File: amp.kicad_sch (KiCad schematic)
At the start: 13 parts, among them J12 JST_SH_1x2_SM02B-SRSS-TB-LF-SN, J9 JST_SUR_1x5_BM05B-SURS-TB-LF-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, U17 MAX98357A

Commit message: [#71249] Update project name
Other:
- title: Audio Latency Processing Board -> Audio controller board
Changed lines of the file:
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@@
 	(paper "A3")
 	(title_block
-		(title "Audio Latency Processing Board")
+		(title "Audio controller board")
 		(date "2025-01-20")
 		(rev "1.2.0")
@@
 		)
 		(instances
-			(project "audio-latency-processing-board"
+			(project "audio-controller-board"
 				(path "/7fb12ebf-f685-4412-b638-445b1bf344bc/80300fa7-dce3-4149-8e27-6609cbfb608d"
 					(reference "R36")
@@
 		)
 		(instances
-			(project "audio-latency-processing-board"
+			(project "audio-controller-board"
 				(path "/7fb12ebf-f685-4412-b638-445b1bf344bc/80300fa7-dce3-4149-8e27-6609cbfb608d"
 					(reference "D10")
@@
 		)
 		(instances
-			(project "audio-latency-processing-board"
+			(project "audio-controller-board"
 				(path "/7fb12ebf-f685-4412-b638-445b1bf344bc/80300fa7-dce3-4149-8e27-6609cbfb608d"
 					(reference "#PWR0138")
@@
 		)
 		(instances
-			(project "audio-latency-processing-board"
+			(project "audio-controller-board"
 				(path "/7fb12ebf-f685-4412-b638-445b1bf344bc/80300fa7-dce3-4149-8e27-6609cbfb608d"
 					(reference "J9")
@@
 		)
 		(instances
-			(project "audio-latency-processing-board"
+			(project "audio-controller-board"
 				(path "/7fb12ebf-f685-4412-b638-445b1bf344bc/80300fa7-dce3-4149-8e27-6609cbfb608d"
 					(reference "#PWR0139")
@@
 		)
 		(instances
-			(project "audio-latency-processing-board"
+			(project "audio-controller-board"
 				(path "/7fb12ebf-f685-4412-b638-445b1bf344bc/80300fa7-dce3-4149-8e27-6609cbfb608d"
 					(reference "#PWR036")
@@
 		)
 		(instances
-			(project "audio-latency-processing-board"
+			(project "audio-controller-board"
 				(path "/7fb12ebf-f685-4412-b638-445b1bf344bc/80300fa7-dce3-4149-8e27-6609cbfb608d"
 					(reference "#PWR0127")
@@
 		)
 		(instances
-			(project "audio-latency-processing-board"
+			(project "audio-controller-board"
 				(path "/7fb12ebf-f685-4412-b638-445b1bf344bc/80300fa7-dce3-4149-8e27-6609cbfb608d"
 					(reference "#PWR033")
@@
 		)
 		(instances
-			(project "audio-latency-processing-board"
+			(project "audio-controller-board"
 				(path "/7fb12ebf-f685-4412-b638-445b1bf344bc/80300fa7-dce3-4149-8e27-6609cbfb608d"
 					(reference "#PWR067")
@@
 		)
 		(instances
-			(project "audio-latency-processing-board"
+			(project "audio-controller-board"
 				(path "/7fb12ebf-f685-4412-b638-445b1bf344bc/80300fa7-dce3-4149-8e27-6609cbfb608d"
 					(reference "D11")
@@
 		)
 		(instances
-			(project "audio-latency-processing-board"
+			(project "audio-controller-board"
 				(path "/7fb12ebf-f685-4412-b638-445b1bf344bc/80300fa7-dce3-4149-8e27-6609cbfb608d"
 					(reference "#PWR0160")
@@
 		)
 		(instances
-			(project "audio-latency-processing-board"
+			(project "audio-controller-board"
 				(path "/7fb12ebf-f685-4412-b638-445b1bf344bc/80300fa7-dce3-4149-8e27-6609cbfb608d"
 					(reference "#PWR041")
@@
 		)
 		(instances
-			(project "audio-latency-processing-board"
+			(project "audio-controller-board"
 				(path "/7fb12ebf-f685-4412-b638-445b1bf344bc/80300fa7-dce3-4149-8e27-6609cbfb608d"
 					(reference "R99")
@@
 		)
 		(instances
-			(project "audio-latency-processing-board"
+			(project "audio-controller-board"
 				(path "/7fb12ebf-f685-4412-b638-445b1bf344bc/80300fa7-dce3-4149-8e27-6609cbfb608d"
 					(reference "#PWR032")
@@
 		)
 		(instances
-			(project "audio-latency-processing-board"
+			(project "audio-controller-board"
 				(path "/7fb12ebf-f685-4412-b638-445b1bf344bc/80300fa7-dce3-4149-8e27-6609cbfb608d"
 					(reference "#PWR0128")
@@
 		)
 		(instances
-			(project "audio-latency-processing-board"
+			(project "audio-controller-board"
 				(path "/7fb12ebf-f685-4412-b638-445b1bf344bc/80300fa7-dce3-4149-8e27-6609cbfb608d"
 					(reference "#PWR0129")
@@
 		)
 		(instances
-			(project "audio-latency-processing-board"
+			(project "audio-controller-board"
 				(path "/7fb12ebf-f685-4412-b638-445b1bf344bc/80300fa7-dce3-4149-8e27-6609cbfb608d"
 					(reference "C53")
@@
 		)
 		(instances
-			(project "audio-latency-processing-board"
+			(project "audio-controller-board"
 				(path "/7fb12ebf-f685-4412-b638-445b1bf344bc/80300fa7-dce3-4149-8e27-6609cbfb608d"
 					(reference "#PWR037")
@@
 		)
 		(instances
-			(project "audio-latency-processing-board"
+			(project "audio-controller-board"
 				(path "/7fb12ebf-f685-4412-b638-445b1bf344bc/80300fa7-dce3-4149-8e27-6609cbfb608d"
 					(reference "#PWR0140")
@@
 		)
 		(instances
-			(project "audio-latency-processing-board"
+			(project "audio-controller-board"
 				(path "/7fb12ebf-f685-4412-b638-445b1bf344bc/80300fa7-dce3-4149-8e27-6609cbfb608d"
 					(reference "R17")
@@
 		)
 		(instances
-			(project "audio-latency-processing-board"
+			(project "audio-controller-board"
 				(path "/7fb12ebf-f685-4412-b638-445b1bf344bc/80300fa7-dce3-4149-8e27-6609cbfb608d"
 					(reference "D12")
@@
 		)
 		(instances
-			(project "audio-latency-processing-board"
+			(project "audio-controller-board"
 				(path "/7fb12ebf-f685-4412-b638-445b1bf344bc/80300fa7-dce3-4149-8e27-6609cbfb608d"
 					(reference "#PWR034")
@@
 		)
 		(instances
-			(project "audio-latency-processing-board"
+			(project "audio-controller-board"
 				(path "/7fb12ebf-f685-4412-b638-445b1bf344bc/80300fa7-dce3-4149-8e27-6609cbfb608d"
 					(reference "#PWR065")

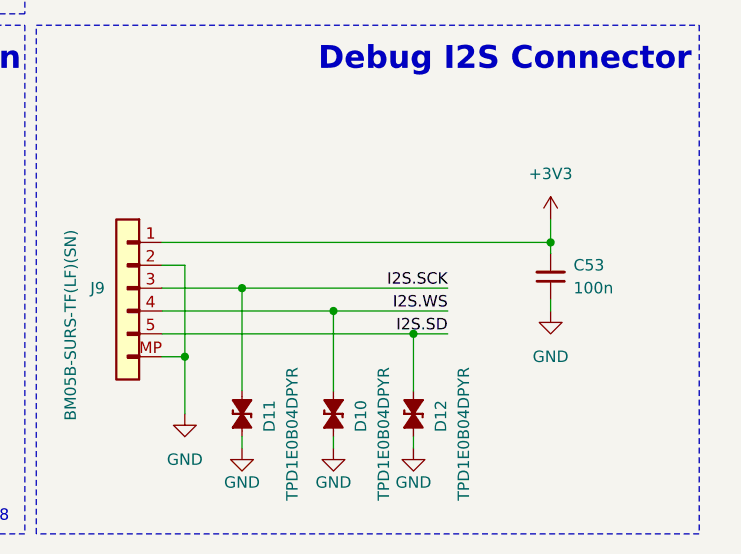
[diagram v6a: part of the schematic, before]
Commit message: [#71230] Replace speaker I2S ESD protection. Route speaker I2S lines
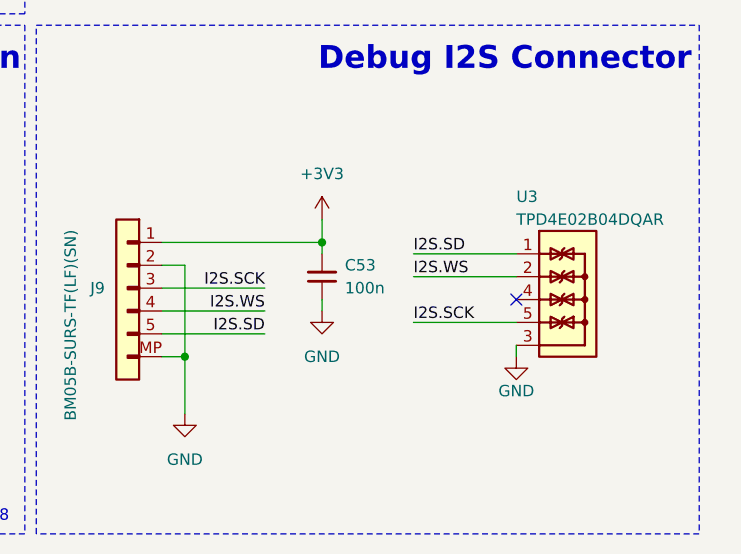
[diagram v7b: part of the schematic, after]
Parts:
- removed D10, D11, D12: TPD1E0B04_XDFN-2, antmicro-footprints:XDFN-2_1x0.60mm, symbol antmicroTVSDiodes:TPD1E0B04_XDFN-2
- added U3: TPD4E02B04DQA, antmicro-footprints:USON-10_2.5x1mm_P0.5mm, symbol antmicroTVSDiodes:TPD4E02B04DQA
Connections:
- net GND: now also U3.3, U3.8
- net I2S.SCK: now also U3.5, U3.6
- net I2S.SD: now also U3.1, U3.10
- net I2S.WS: now also U3.2, U3.9
- new net: U3.4, U3.7
- no-connect marks 0 -> 1
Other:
- moved on the sheet: C53
